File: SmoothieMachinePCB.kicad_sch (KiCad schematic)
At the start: 18 parts, among them J1 Conn_01x02, J2 Conn_01x02, J3 Conn_01x02, J4 Conn_01x02, U1 ESP32-S3-WROOM-2, U2 LM1117MP-3.3

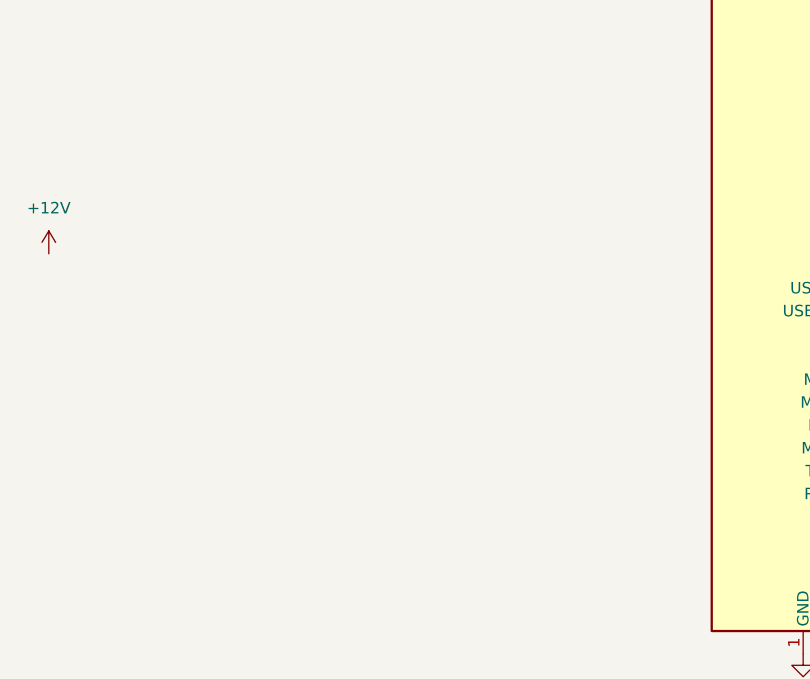
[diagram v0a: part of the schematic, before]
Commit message: Added motor driver
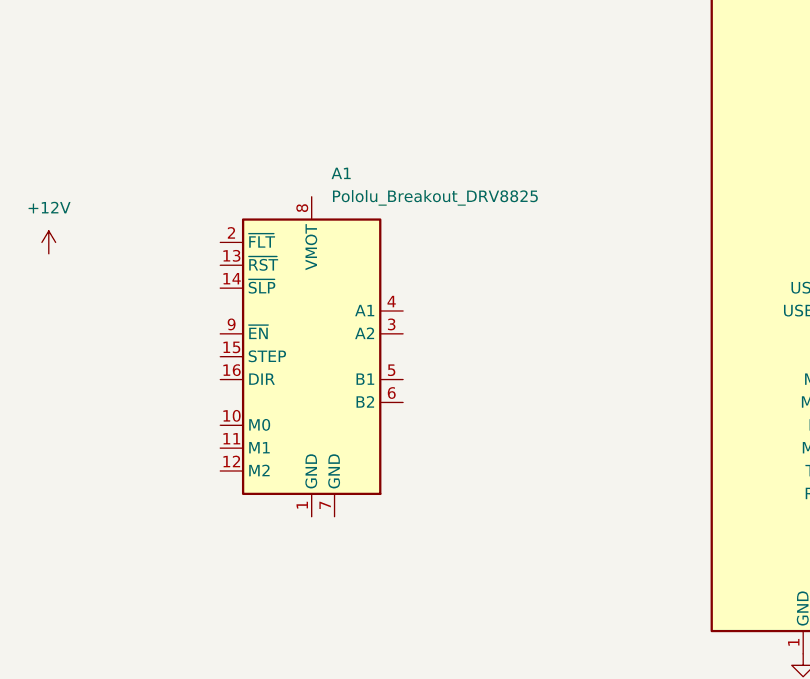
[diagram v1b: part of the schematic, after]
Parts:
- added A1: Pololu_Breakout_DRV8825, Module:Pololu_Breakout-16_15.2x20.3mm, symbol Driver_Motor:Pololu_Breakout_DRV8825
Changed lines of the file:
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@@
+	)
+	(symbol
+		(lib_id "Driver_Motor:Pololu_Breakout_DRV8825")
+		(at 71.12 99.06 0)
+		(unit 1)
+		(exclude_from_sim no)
+		(in_bom yes)
+		(on_board yes)
+		(dnp no)
+		(fields_autoplaced yes)
+		(property "Reference" "A1"
+			(at 73.3141 81.28 0)
+			(effects
+				(font
+					(size 1.27 1.27)
+				)
+				(justify left)
+			)
+		)
+		(property "Value" "Pololu_Breakout_DRV8825"
+			(at 73.3141 83.82 0)
+			(effects
+				(font
+					(size 1.27 1.27)
+				)
+				(justify left)
+			)
+		)
+		(property "Footprint" "Module:Pololu_Breakout-16_15.2x20.3mm"
+			(at 76.2 119.38 0)
+			(effects
+				(font
+					(size 1.27 1.27)
+				)
+				(justify left)
+				(hide yes)
+			)
+		)
+		(property "Datasheet" "https://www.pololu.com/product/2982"
+			(at 73.66 106.68 0)
+			(effects
+				(font
+					(size 1.27 1.27)
+				)
+				(hide yes)
+			)
+		)
+		(property "Description" "Pololu Breakout Board, Stepper Driver DRV8825"
+			(at 71.12 99.06 0)
+			(effects
+				(font
+					(size 1.27 1.27)
+				)
+				(hide yes)
+			)
+		)
+		(pin "12"
+		)
+		(pin "9"
+		)
+		(pin "3"
+		)
+		(pin "4"
+		)
+		(pin "11"
+		)
+		(pin "7"
+		)
+		(pin "6"
+		)
+		(pin "16"
+		)
+		(pin "15"
+		)
+		(pin "1"
+		)
+		(pin "13"
+		)
+		(pin "5"
+		)
+		(pin "14"
+		)
+		(pin "8"
+		)
+		(pin "10"
+		)
+		(pin "2"
+		)
+		(instances
+			(project ""
+				(path "/0378f42a-d7c1-4f1b-8fcb-b5ba01b86579"
+					(reference "A1")
+					(unit 1)
+				)
+			)
+		)
 	)
 	(symbol

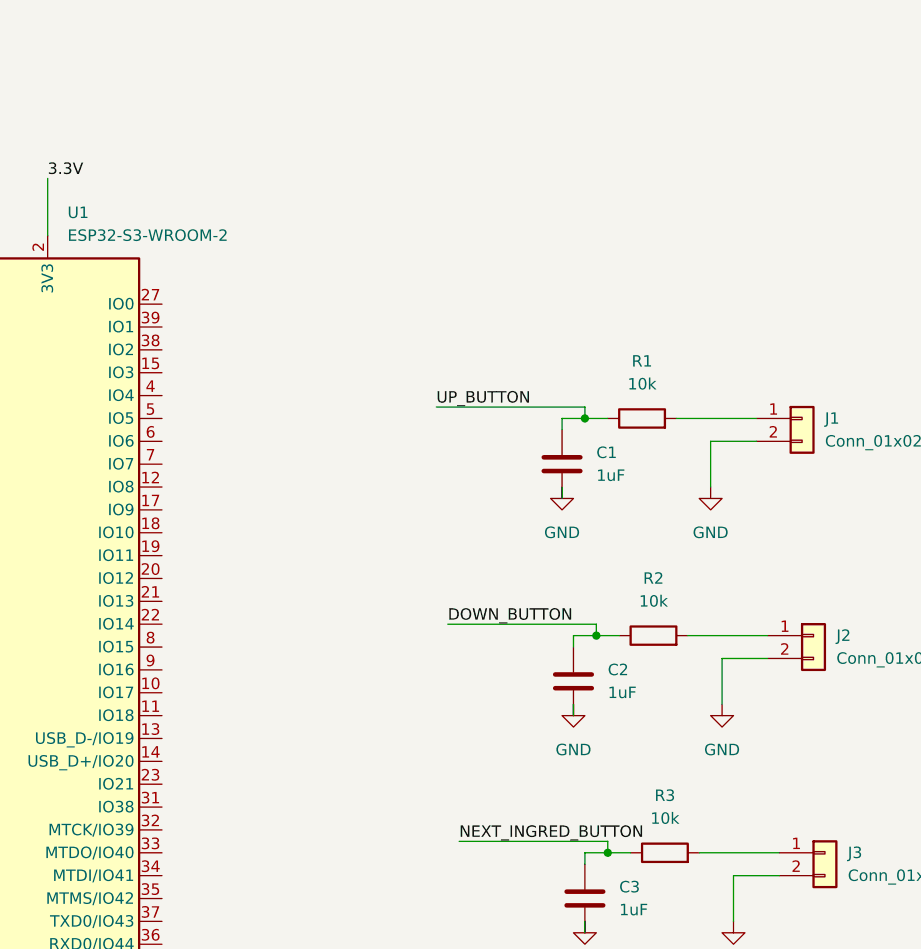
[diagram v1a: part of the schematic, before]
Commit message: Added LED
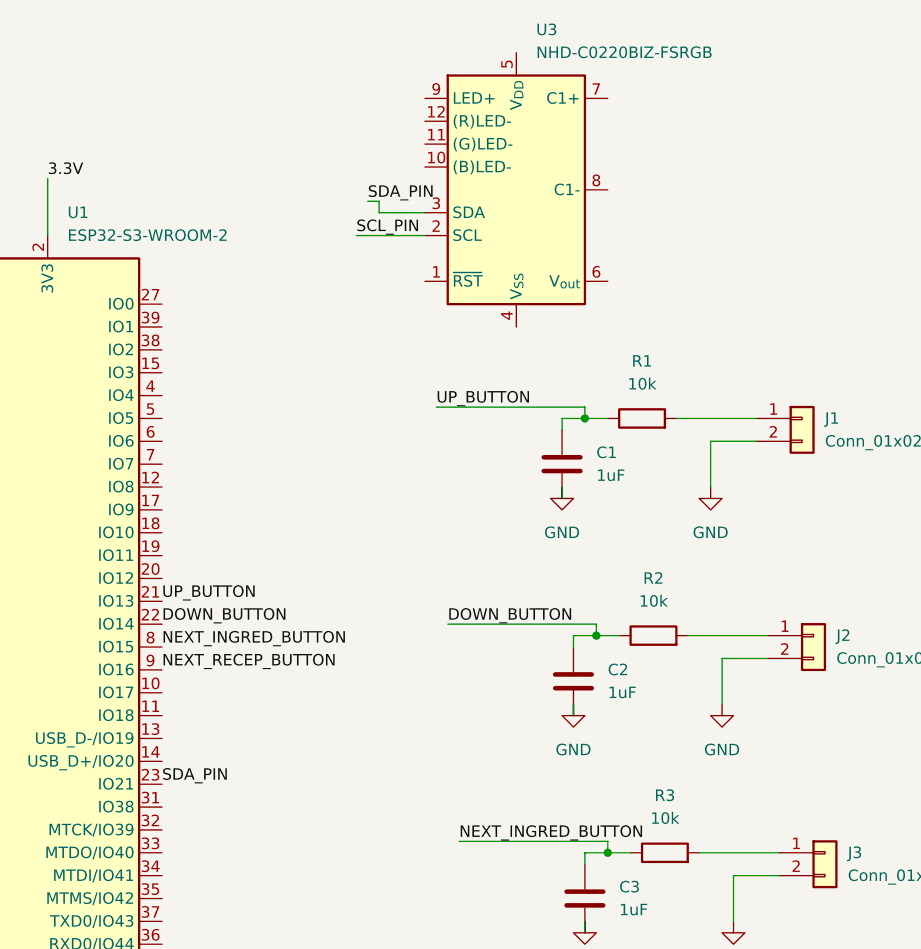
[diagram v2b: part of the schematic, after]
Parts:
- added U3: NHD-C0220BIZ-FSRGB, Display:NHD-C0220BiZ-FSRGB, symbol Display_Character:NHD-C0220BIZ-FSRGB
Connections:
- net DOWN_BUTTON: now also U1.22 (IO14)
- net NEXT_INGRED_BUTTON: now also U1.8 (IO15)
- net NEXT_RECEP_BUTTON: now also U1.9 (IO16)
- net UP_BUTTON: now also U1.21 (IO13)
- net SDA_PIN: now reaches U1.23 (IO21)
- net SDA_PIN: now also U3.3 (SDA)
- new net SCL_PIN: U3.2 (SCL)
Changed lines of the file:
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@@
+	(wire
+		(pts
+			(xy 161.29 34.29) (xy 162.56 34.29)
+		)
+		(stroke
+			(width 0)
+			(type default)
+		)
+	)
+	(wire
+		(pts
+			(xy 162.56 35.56) (xy 167.64 35.56)
+		)
+		(stroke
+			(width 0)
+			(type default)
+		)
+	)
 	(wire
 		(pts
@@
 	(wire
 		(pts
+			(xy 160.02 38.1) (xy 167.64 38.1)
+		)
+		(stroke
+			(width 0)
+			(type default)
+		)
+	)
+	(wire
+		(pts
 			(xy 186.69 82.55) (xy 189.23 82.55)
 		)
@@
 		(pts
 			(xy 125.73 31.75) (xy 125.73 38.1)
+		)
+		(stroke
+			(width 0)
+			(type default)
+		)
+	)
+	(wire
+		(pts
+			(xy 162.56 34.29) (xy 162.56 35.56)
 		)
 		(stroke
@@
 		)
 	)
+	(label "DOWN_BUTTON"
+		(at 138.43 81.28 0)
+		(effects
+			(font
+				(size 1.27 1.27)
+			)
+			(justify left bottom)
+		)
+	)
+	(label "SCL_PIN"
+		(at 160.02 38.1 0)
+		(effects
+			(font
+				(size 1.27 1.27)
+			)
+			(justify left bottom)
+		)
+	)
 	(label "NEXT_INGRED_BUTTON"
 		(at 171.45 105.41 0)
@@
 		)
 	)
+	(label "SDA_PIN"
+		(at 138.43 99.06 0)
+		(effects
+			(font
+				(size 1.27 1.27)
+			)
+			(justify left bottom)
+		)
+	)
+	(label "NEXT_INGRED_BUTTON"
+		(at 138.43 83.82 0)
+		(effects
+			(font
+				(size 1.27 1.27)
+			)
+			(justify left bottom)
+		)
+	)
 	(label "UP_BUTTON"
 		(at 168.91 57.15 0)
@@
 		)
 	)
+	(label "SDA_PIN"
+		(at 161.29 34.29 0)
+		(effects
+			(font
+				(size 1.27 1.27)
+			)
+			(justify left bottom)
+		)
+	)
+	(label "NEXT_RECEP_BUTTON"
+		(at 138.43 86.36 0)
+		(effects
+			(font
+				(size 1.27 1.27)
+			)
+			(justify left bottom)
+		)
+	)
 	(label "VDD33"
 		(at 67.31 33.02 0)
+		(effects
+			(font
+				(size 1.27 1.27)
+			)
+			(justify left bottom)
+		)
+	)
+	(label "UP_BUTTON"
+		(at 138.43 78.74 0)
 		(effects
 			(font
@@
 					(unit 1)
 				)
+			)
+		)
+	)
+	(symbol
+		(lib_id "Display_Character:NHD-C0220BIZ-FSRGB")
+		(at 177.8 33.02 0)
+		(unit 1)
+		(exclude_from_sim no)
+		(in_bom yes)
+		(on_board yes)
+		(dnp no)
+		(fields_autoplaced yes)
+		(property "Reference" "U3"
+			(at 179.9941 15.24 0)
+			(effects
+				(font
+					(size 1.27 1.27)
+				)
+				(justify left)
+			)
+		)
+		(property "Value" "NHD-C0220BIZ-FSRGB"
+			(at 179.9941 17.78 0)
+			(effects
+				(font
+					(size 1.27 1.27)
+				)
+				(justify left)
+			)
+		)
+		(property "Footprint" "Display:NHD-C0220BiZ-FSRGB"
+			(at 177.8 35.56 0)
+			(effects
+				(font
+					(size 1.27 1.27)
+					(italic yes)
+				)
+				(hide yes)
+			)
+		)
+		(property "Datasheet" "https://newhavendisplay.com/content/specs/NHD-C0220BiZ-FSRGB-FBW-3VM.pdf"
+			(at 177.8 33.02 0)
+			(effects
+				(font
+					(size 1.27 1.27)
+					(italic yes)
+				)
+				(hide yes)
+			)
+		)
+		(property "Description" "2x20 character LCD module with common anode RGB backlight, I2C, 3.3V"
+			(at 177.8 33.02 0)
+			(effects
+				(font
+					(size 1.27 1.27)
+				)
+				(hide yes)
+			)
+		)
+		(pin "3"
+		)
+		(pin "12"
+		)
+		(pin "7"
+		)
+		(pin "8"
+		)
+		(pin "11"
+		)
+		(pin "9"
+		)
+		(pin "10"
+		)
+		(pin "2"
+		)
+		(pin "5"
+		)
+		(pin "6"
+		)
+		(pin "4"
+		)
+		(pin "1"
+		)
+		(instances
+			(project ""
+				(path "/0378f42a-d7c1-4f1b-8fcb-b5ba01b86579"
+					(reference "U3")
+					(unit 1)
+				)

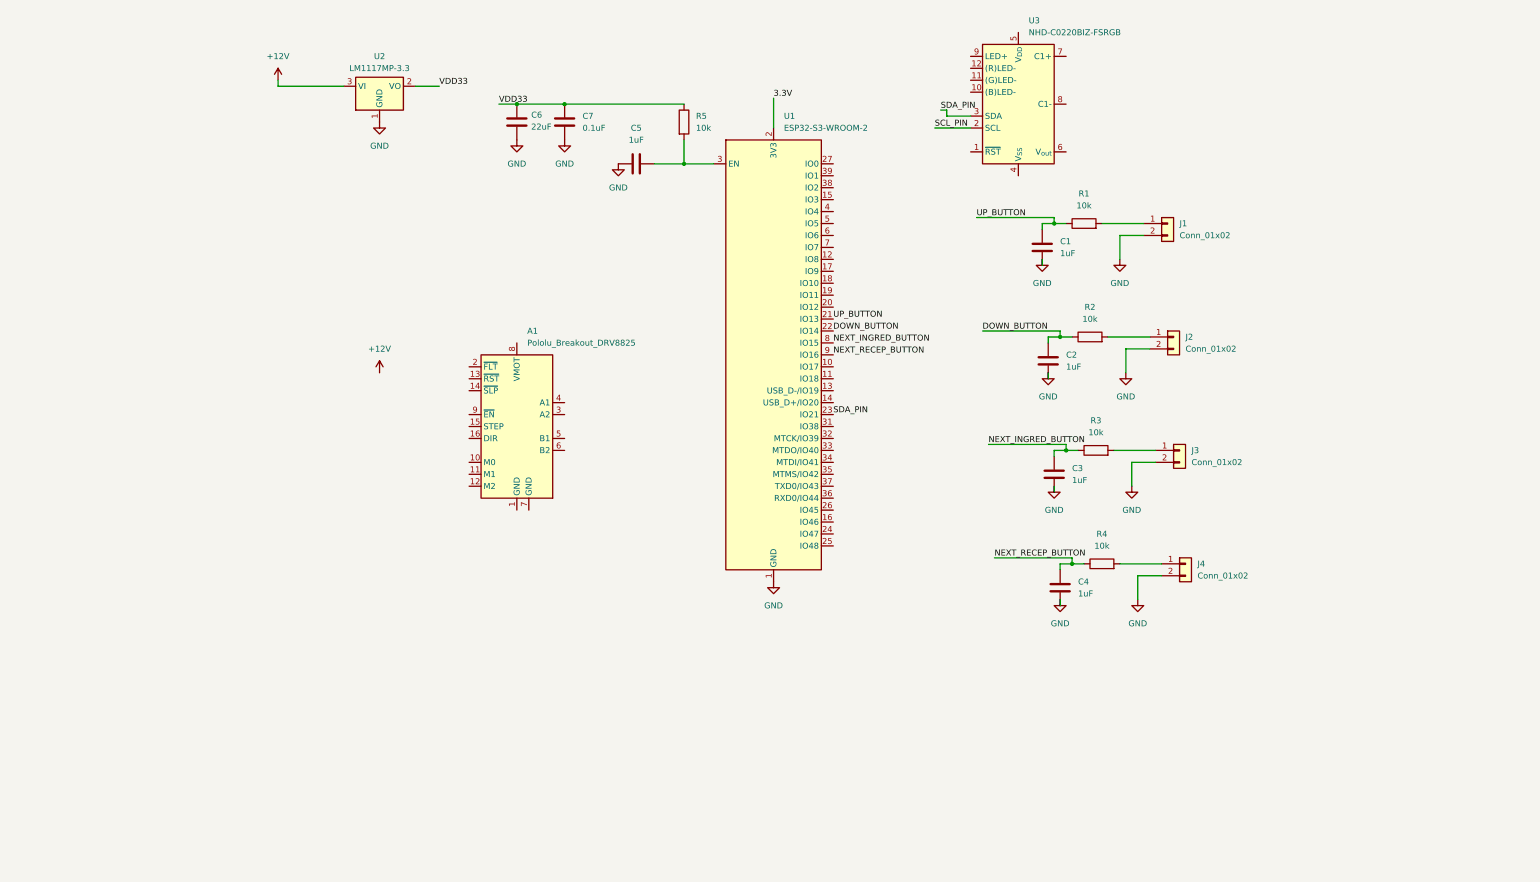
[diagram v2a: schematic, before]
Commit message: First basically complete schematic of PCB
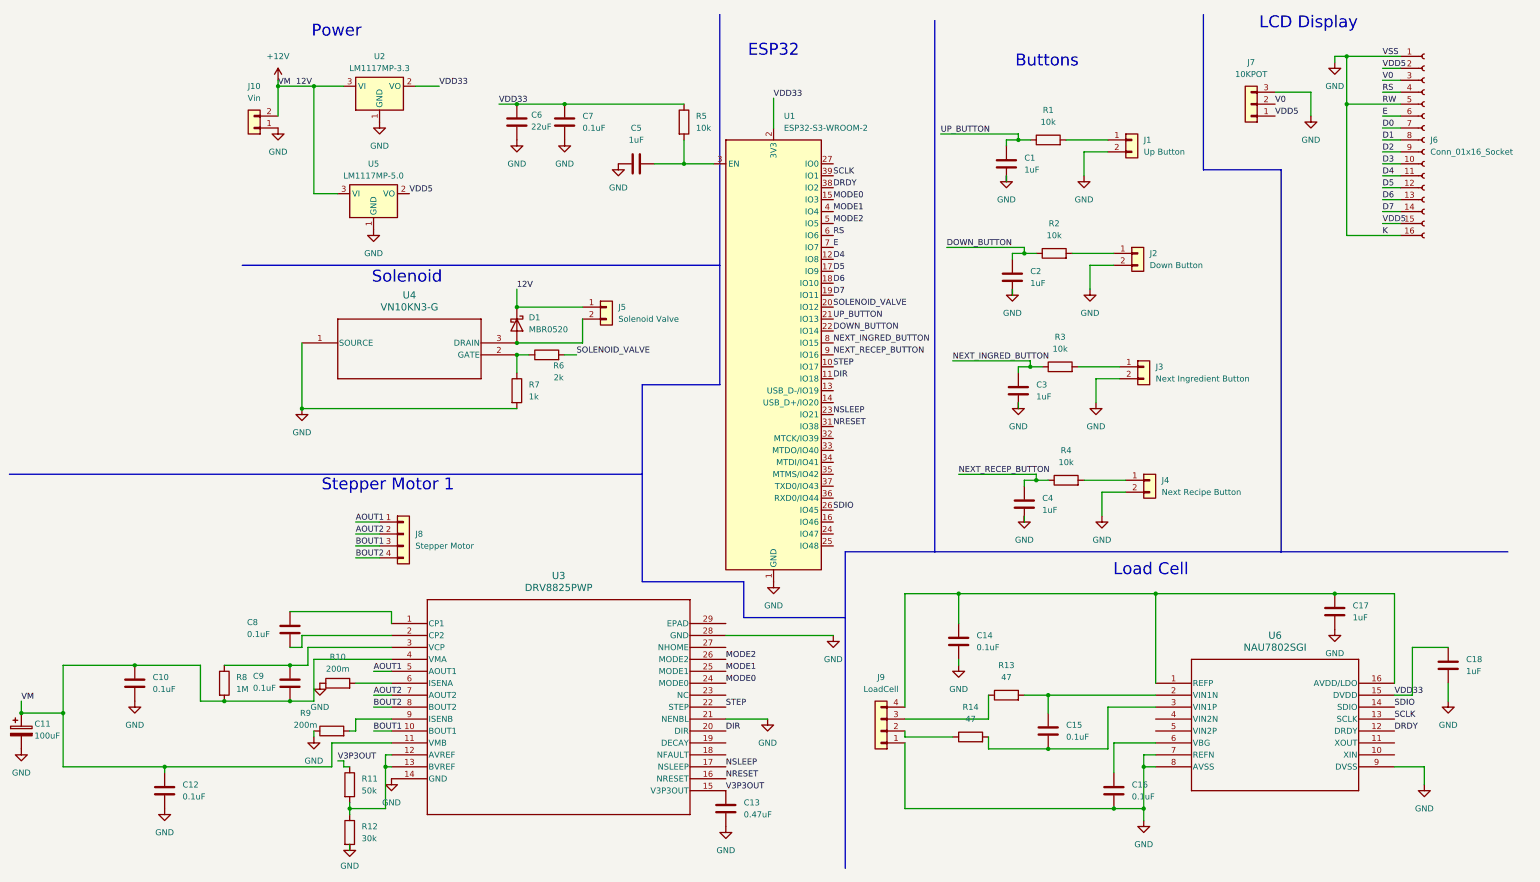
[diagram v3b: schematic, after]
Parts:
- removed A1: Pololu_Breakout_DRV8825, Module:Pololu_Breakout-16_15.2x20.3mm, symbol Driver_Motor:Pololu_Breakout_DRV8825
- removed U3: NHD-C0220BIZ-FSRGB, Display:NHD-C0220BiZ-FSRGB, symbol Display_Character:NHD-C0220BIZ-FSRGB
- added C10, C12, C14, C15, C16, C8, C9: 0.1uF, symbol Device:C
- added C11: 100uF, symbol Device:C_Polarized
- added C13: 0.47uF, symbol Device:C
- added C17, C18: 1uF, symbol Device:C
- added D1: MBR0520, Diode_SMD:D_SOD-123, symbol Diode:MBR0520
- added J10: Vin, symbol Connector_Generic:Conn_01x02
- added J5: Solenoid Valve, symbol Connector_Generic:Conn_01x02
- added J6: Conn_01x16_Socket, symbol Connector:Conn_01x16_Socket
- added J7: 10KPOT, symbol Connector_Generic:Conn_01x03
- added J8: Stepper Motor, symbol Connector_Generic:Conn_01x04
- added J9: LoadCell, symbol Connector_Generic:Conn_01x04
- added R10, R9: 200m, symbol Device:R
- added R11: 50k, symbol Device:R
- added R12: 30k, symbol Device:R
- added R13, R14: 47, symbol Device:R
- added R6: 2k, symbol Device:R
- added R7: 1k, symbol Device:R
- added R8: 1M, symbol Device:R
- added U3: DRV8825PWP, PWP28_5P18X3P1, symbol DRV8825PWP:DRV8825PWP
- added U4: VN10KN3-G, TO-92_MC_MCH, symbol VN10KN3-G:VN10KN3-G
- added U5: LM1117MP-5.0, Package_TO_SOT_SMD:SOT-223-3_TabPin2, symbol Regulator_Linear:LM1117MP-5.0
- added U6: NAU7802SGI, SOI16_NAU7802SGI_NUV, symbol NAU7802SGI:NAU7802SGI
- J1: value Conn_01x02 -> Up Button
- J2: value Conn_01x02 -> Down Button
- J3: value Conn_01x02 -> Next Ingredient Button
- J4: value Conn_01x02 -> Next Recipe Button
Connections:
- net 3.3V is gone; now on net VDD33: U1.2 (3V3)
- net +12V: now also C10.1, C11.1, C12.1, C9.2, D1.1 (K), J10.2 (Pin_2), J5.1 (Pin_1), R8.2, U3.11 (VMB), U3.4 (VMA), U5.3 (VI)
- net GND: now also C10.2, C11.2, C12.2, C13.2, C14.2, C16.2, C17.2, C18.2, J10.1 (Pin_1), J6.1 (Pin_1), J6.16 (Pin_16), J6.5 (Pin_5), J7.3 (Pin_3), J9.1 (Pin_1), R10.1, R12.2, R7.2, R9.1, U3.14 (GND), U3.21 (NENBL), U3.28 (GND), U4.1 (SOURCE), U5.1 (GND), U6.7 (REFN), U6.8 (AVSS), U6.9 (DVSS)
- net VDD33: now also C18.1, U6.15 (DVDD)
- net STEP: now reaches U1.10 (IO17)
- net STEP: now also U3.22 (STEP)
- net DIR: now reaches U1.11 (IO18)
- net DIR: now also U3.20 (DIR)
- net D4: now reaches U1.12 (IO8)
- net D4: now also J6.11 (Pin_11)
- net MODE0: now reaches U1.15 (IO3)
- net MODE0: now also U3.24 (MODE0)
- net D5: now reaches U1.17 (IO9)
- net D5: now also J6.12 (Pin_12)
- net D6: now reaches U1.18 (IO10)
- net D6: now also J6.13 (Pin_13)
- net D7: now reaches U1.19 (IO11)
- net D7: now also J6.14 (Pin_14)
- net SOLENOID_VALVE: now reaches U1.20 (IO12)
- net SOLENOID_VALVE: now also R6.2
- net SDIO: now reaches U1.26 (IO45)
- net SDIO: now also U6.14 (SDIO)
- net NRESET: now reaches U1.31 (IO38)
- net NRESET: now also U3.16 (NRESET)
- net DRDY: now reaches U1.38 (IO2)
- net DRDY: now also U6.12 (DRDY)
- net SCLK: now reaches U1.39 (IO1)
- net SCLK: now also U6.13 (SCLK)
- net MODE1: now reaches U1.4 (IO4)
- net MODE1: now also U3.25 (MODE1)
- net MODE2: now reaches U1.5 (IO5)
- net MODE2: now also U3.26 (MODE2)
- net RS: now reaches U1.6 (IO6)
- net RS: now also J6.4 (Pin_4)
- net E: now reaches U1.7 (IO7)
- net E: now also J6.6 (Pin_6)
- net SDA_PIN renamed NSLEEP
- net NSLEEP: now also U3.17 (NSLEEP)
- new net: C9.1, R8.1, U3.3 (VCP)
- new net: C14.1, C17.1, J9.4 (Pin_4), U6.1 (REFP), U6.16 (AVDD/LDO)
- new net: J9.2 (Pin_2), R14.1
- new net: J9.3 (Pin_3), R13.1
- new net: C15.1, R13.2, U6.2 (VIN1N)
- new net: C15.2, R14.2, U6.3 (VIN1P)
- new net: C16.1, U6.6 (VBG)
- new net: C8.1, U3.1 (CP1)
- new net: C8.2, U3.2 (CP2)
- new net: R11.2, R12.1, U3.12 (AVREF), U3.13 (BVREF)
- new net: R10.2, U3.6 (ISENA)
- new net: R9.2, U3.9 (ISENB)
- new net: R6.1, R7.1, U4.2 (GATE)
- new net: D1.2 (A), J5.2 (Pin_2), U4.3 (DRAIN)
- new net AOUT1: J8.1 (Pin_1), U3.5 (AOUT1)
- new net AOUT2: J8.2 (Pin_2), U3.7 (AOUT2)
- new net BOUT1: J8.3 (Pin_3), U3.10 (BOUT1)
- new net BOUT2: J8.4 (Pin_4), U3.8 (BOUT2)
- new net D0: J6.7 (Pin_7)
- new net D1: J6.8 (Pin_8)
- new net D2: J6.9 (Pin_9)
- new net D3: J6.10 (Pin_10)
- new net V0: J6.3 (Pin_3), J7.2 (Pin_2)
- new net V3P3OUT: C13.1, R11.1, U3.15 (V3P3OUT)
- new net VDD5: J6.15 (Pin_15), J6.2 (Pin_2), J7.1 (Pin_1), U5.2 (VO)
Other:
- note added: "Buttons"
- note added: "ESP32"
- note added: "LCD Display"
- note added: "Load Cell"
- note added: "Power"
- note added: "Solenoid"
- note added: "Stepper Motor 1"
- moved on the sheet: C1, C2, C3, C4, J1, J2, J3, J4, R1, R2, R3, R4
